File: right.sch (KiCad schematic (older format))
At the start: 59 parts, among them J10 UTC16-G, J4 reset, J5 Speaker, J6 ISP, J8 Sig, P6 WS2812, P8 SJ-43514-SMT, SW25 Socket, SW26 Socket, SW27 Socket, SW28 Socket, SW29 Socket, SW30 Socket, SW31 Socket, SW32 Socket, SW33 Socket, SW34 Socket, SW35 Socket, SW36 Socket, SW37 Socket, SW38 Socket, SW39 Socket, SW40 Socket, SW41 Socket, SW42 Socket, SW43 Socket, SW44 Socket, SW45 Socket, SW46 Socket, SW47 Socket, SW48 Socket, SW50 FSMSM, U2 ATMega32U4, Y2 16MHz

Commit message: Added WS2812B leds to one half
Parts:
- added C? (x6): 1uF, Capacitor_SMD:C_0603_1608Metric, symbol vitamins_included-rescue:C_Small-RESCUE-lets_split_panel-lets_split_panel-rescue
- added D? (x6): WS2812B, LED_SMD:LED_WS2812B_PLCC4_5.0x5.0mm_P3.2mm, symbol LED:WS2812B
- J10: symbol Connector:USB_C_Receptacle -> vitamins_included-rescue:USB_C_Receptacle-Connector
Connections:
- wire segments 187 -> 244

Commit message: started work on second half
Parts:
- gave numbers to parts that had none: 12
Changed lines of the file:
@@
 U 1 1 5C305AB7
 P 7800 4400
-F 0 "D?" H 7875 4650 50  0000 L CNN
+AR Path="/5A0DE9BD/5C305AB7" Ref="D?"  Part="1"
+AR Path="/5A0DF911/5C305AB7" Ref="D35"  Part="1"
+F 0 "D35" H 7875 4650 50  0000 L CNN
 F 1 "WS2812B" H 7875 4150 50  0000 L CNN
 F 2 "LED_SMD:LED_WS2812B_PLCC4_5.0x5.0mm_P3.2mm" H 7850 4100 50  0001 L TNN
@@
 U 1 1 5C305ABE
 P 7350 4200
-F 0 "C?" H 7442 4246 50  0000 L CNN
+AR Path="/5A0DE9BD/5C305ABE" Ref="C?"  Part="1"
+AR Path="/5A0DF911/5C305ABE" Ref="C15"  Part="1"
+F 0 "C15" H 7442 4246 50  0000 L CNN
 F 1 "1uF" H 7442 4155 50  0000 L CNN
 F 2 "Capacitor_SMD:C_0603_1608Metric" H 7350 4200 50  0001 C CNN
@@
 U 1 1 5C305ACC
 P 8750 4400
-F 0 "D?" H 8825 4650 50  0000 L CNN
+AR Path="/5A0DE9BD/5C305ACC" Ref="D?"  Part="1"
+AR Path="/5A0DF911/5C305ACC" Ref="D36"  Part="1"
+F 0 "D36" H 8825 4650 50  0000 L CNN
 F 1 "WS2812B" H 8825 4150 50  0000 L CNN
 F 2 "LED_SMD:LED_WS2812B_PLCC4_5.0x5.0mm_P3.2mm" H 8800 4100 50  0001 L TNN
@@
 U 1 1 5C305AD3
 P 8300 4200
-F 0 "C?" H 8392 4246 50  0000 L CNN
+AR Path="/5A0DE9BD/5C305AD3" Ref="C?"  Part="1"
+AR Path="/5A0DF911/5C305AD3" Ref="C16"  Part="1"
+F 0 "C16" H 8392 4246 50  0000 L CNN
 F 1 "1uF" H 8392 4155 50  0000 L CNN
 F 2 "Capacitor_SMD:C_0603_1608Metric" H 8300 4200 50  0001 C CNN
@@
 U 1 1 5C305AE1
 P 9700 4400
-F 0 "D?" H 9775 4650 50  0000 L CNN
+AR Path="/5A0DE9BD/5C305AE1" Ref="D?"  Part="1"
+AR Path="/5A0DF911/5C305AE1" Ref="D37"  Part="1"
+F 0 "D37" H 9775 4650 50  0000 L CNN
 F 1 "WS2812B" H 9775 4150 50  0000 L CNN
 F 2 "LED_SMD:LED_WS2812B_PLCC4_5.0x5.0mm_P3.2mm" H 9750 4100 50  0001 L TNN
@@
 U 1 1 5C305AE8
 P 9250 4200
-F 0 "C?" H 9342 4246 50  0000 L CNN
+AR Path="/5A0DE9BD/5C305AE8" Ref="C?"  Part="1"
+AR Path="/5A0DF911/5C305AE8" Ref="C17"  Part="1"
+F 0 "C17" H 9342 4246 50  0000 L CNN
 F 1 "1uF" H 9342 4155 50  0000 L CNN
 F 2 "Capacitor_SMD:C_0603_1608Metric" H 9250 4200 50  0001 C CNN
@@
 U 1 1 5C305AF6
 P 7800 5600
-F 0 "D?" H 7875 5850 50  0000 L CNN
+AR Path="/5A0DE9BD/5C305AF6" Ref="D?"  Part="1"
+AR Path="/5A0DF911/5C305AF6" Ref="D38"  Part="1"
+F 0 "D38" H 7875 5850 50  0000 L CNN
 F 1 "WS2812B" H 7875 5350 50  0000 L CNN
 F 2 "LED_SMD:LED_WS2812B_PLCC4_5.0x5.0mm_P3.2mm" H 7850 5300 50  0001 L TNN
@@
 U 1 1 5C305AFD
 P 7350 5400
-F 0 "C?" H 7442 5446 50  0000 L CNN
+AR Path="/5A0DE9BD/5C305AFD" Ref="C?"  Part="1"
+AR Path="/5A0DF911/5C305AFD" Ref="C18"  Part="1"
+F 0 "C18" H 7442 5446 50  0000 L CNN
 F 1 "1uF" H 7442 5355 50  0000 L CNN
 F 2 "Capacitor_SMD:C_0603_1608Metric" H 7350 5400 50  0001 C CNN
@@
 U 1 1 5C305B09
 P 8750 5600
-F 0 "D?" H 8825 5850 50  0000 L CNN
+AR Path="/5A0DE9BD/5C305B09" Ref="D?"  Part="1"
+AR Path="/5A0DF911/5C305B09" Ref="D39"  Part="1"
+F 0 "D39" H 8825 5850 50  0000 L CNN
 F 1 "WS2812B" H 8825 5350 50  0000 L CNN
 F 2 "LED_SMD:LED_WS2812B_PLCC4_5.0x5.0mm_P3.2mm" H 8800 5300 50  0001 L TNN
@@
 U 1 1 5C305B10
 P 8300 5400
-F 0 "C?" H 8392 5446 50  0000 L CNN
+AR Path="/5A0DE9BD/5C305B10" Ref="C?"  Part="1"
+AR Path="/5A0DF911/5C305B10" Ref="C19"  Part="1"
+F 0 "C19" H 8392 5446 50  0000 L CNN
 F 1 "1uF" H 8392 5355 50  0000 L CNN
 F 2 "Capacitor_SMD:C_0603_1608Metric" H 8300 5400 50  0001 C CNN
@@
 U 1 1 5C305B1E
 P 9700 5600
-F 0 "D?" H 9775 5850 50  0000 L CNN
+AR Path="/5A0DE9BD/5C305B1E" Ref="D?"  Part="1"
+AR Path="/5A0DF911/5C305B1E" Ref="D40"  Part="1"
+F 0 "D40" H 9775 5850 50  0000 L CNN
 F 1 "WS2812B" H 9775 5350 50  0000 L CNN
 F 2 "LED_SMD:LED_WS2812B_PLCC4_5.0x5.0mm_P3.2mm" H 9750 5300 50  0001 L TNN
@@
 U 1 1 5C305B25
 P 9250 5400
-F 0 "C?" H 9342 5446 50  0000 L CNN
+AR Path="/5A0DE9BD/5C305B25" Ref="C?"  Part="1"
+AR Path="/5A0DF911/5C305B25" Ref="C20"  Part="1"
+F 0 "C20" H 9342 5446 50  0000 L CNN
 F 1 "1uF" H 9342 5355 50  0000 L CNN
 F 2 "Capacitor_SMD:C_0603_1608Metric" H 9250 5400 50  0001 C CNN
@@
 U 1 1 5C305B43
 P 7350 4000
-F 0 "#PWR?" H 7350 3850 50  0001 C CNN
+AR Path="/5A0DE9BD/5C305B43" Ref="#PWR?"  Part="1"
+AR Path="/5A0DF911/5C305B43" Ref="#PWR0107"  Part="1"
+F 0 "#PWR0107" H 7350 3850 50  0001 C CNN
 F 1 "VCC" H 7350 4150 50  0000 C CNN
 F 2 "" H 7350 4000 50  0000 C CNN
@@
 U 1 1 5C305B4B
 P 7350 5225
-F 0 "#PWR?" H 7350 5075 50  0001 C CNN
+AR Path="/5A0DE9BD/5C305B4B" Ref="#PWR?"  Part="1"
+AR Path="/5A0DF911/5C305B4B" Ref="#PWR0108"  Part="1"
+F 0 "#PWR0108" H 7350 5075 50  0001 C CNN
 F 1 "VCC" H 7350 5375 50  0000 C CNN
 F 2 "" H 7350 5225 50  0000 C CNN
@@
 U 1 1 5C305B54
 P 7350 6000
-F 0 "#PWR?" H 7350 5750 50  0001 C CNN
+AR Path="/5A0DE9BD/5C305B54" Ref="#PWR?"  Part="1"
+AR Path="/5A0DF911/5C305B54" Ref="#PWR0109"  Part="1"
+F 0 "#PWR0109" H 7350 5750 50  0001 C CNN
 F 1 "GND" H 7350 5850 50  0000 C CNN
 F 2 "" H 7350 6000 50  0000 C CNN
@@
 U 1 1 5C305B5C
 P 7350 4800
-F 0 "#PWR?" H 7350 4550 50  0001 C CNN
+AR Path="/5A0DE9BD/5C305B5C" Ref="#PWR?"  Part="1"
+AR Path="/5A0DF911/5C305B5C" Ref="#PWR0110"  Part="1"
+F 0 "#PWR0110" H 7350 4550 50  0001 C CNN
 F 1 "GND" H 7350 4650 50  0000 C CNN
 F 2 "" H 7350 4800 50  0000 C CNN

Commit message: Fixed rotated LEDs, added config jumpers
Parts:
- removed J10: UTC16-G, Connector_USB:USB_C_Receptacle_Palconn_UTC16-G, symbol vitamins_included-rescue:USB_C_Receptacle-Connector
- removed J5: Speaker, Buzzers_Beepers:Buzzer_12x9.5RM7.6, symbol vitamins_included-rescue:Conn_01x02-RESCUE-lets_split_panel-lets_split_panel-re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
- removed J8: Sig, Pin_Headers:Pin_Header_Straight_1x01_Pitch2.54mm, symbol vitamins_included-rescue:Conn_01x01-RESCUE-lets_split_panel-lets_split_panel-re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
- removed P8: SJ-43514-SMT, Connectors:SJ-4351X-SMT, symbol vitamins_included-rescue:Conn_01x04-RESCUE-lets_split_panel-lets_split_panel-re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
- added J10: UTC16-G, Connector_USB:USB_C_Receptacle_Palconn_UTC16-G, symbol Connector:USB_C_Receptacle_USB2.0
- added J5: Buzzer, Buzzers_Beepers:Buzzer_12x9.5RM7.6, symbol Device:Buzzer
- added JP3: WS_MODE, Jumper:SolderJumper-3_P1.3mm_Bridged12_RoundedPad1.0x1.5mm, symbol Jumper:SolderJumper_3_Bridged12
- added JP6: WS_OUT, Jumper:SolderJumper-3_P1.3mm_Bridged12_RoundedPad1.0x1.5mm, symbol Jumper:SolderJumper_3_Bridged12
- added P8: SJ-43514-SMT, UJ31-CH-31-SMT-TR:SJ-4351X-SMT, symbol Connector:AudioJack4
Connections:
- net labels added: WD2812-out
- wire segments 244 -> 239
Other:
- moved on the sheet: C15, C16, C17, C18, C19, C20, D35, D36, D37, D38, D39, D40

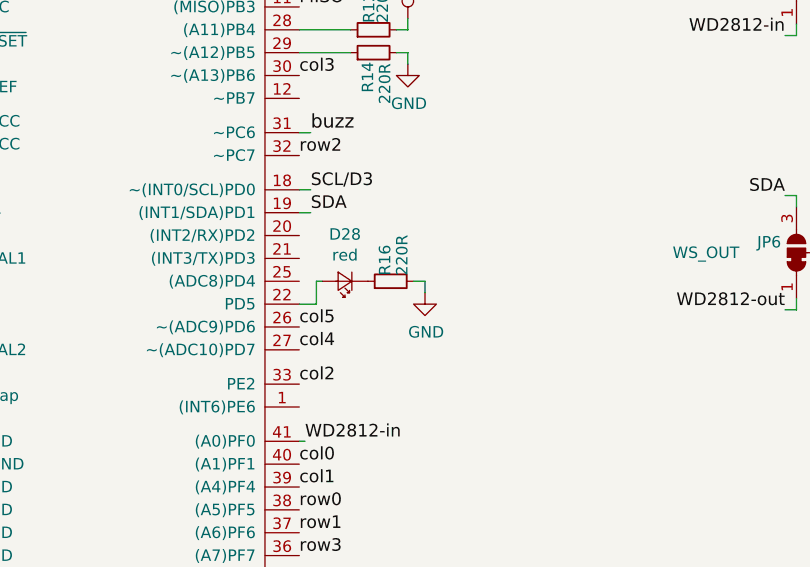
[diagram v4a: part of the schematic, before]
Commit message: Added MPN to DFU LED
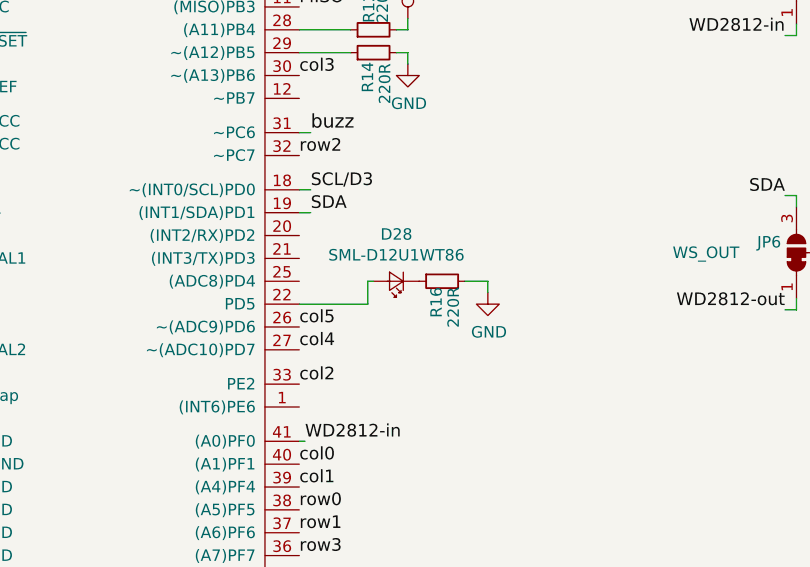
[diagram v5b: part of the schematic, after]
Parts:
- D28: value red -> SML-D12U1WT86
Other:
- moved on the sheet: D28, R16
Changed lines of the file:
@@
 L Device:LED_Small D28
 U 1 1 5B5FD568
-P 5300 5550
-F 0 "D28" H 5300 5345 50  0000 C CNN
-F 1 "red" H 5300 5436 50  0000 C CNN
-F 2 "LED_SMD:LED_0603_1608Metric_Castellated" V 5300 5550 50  0001 C CNN
-F 3 "~" V 5300 5550 50  0001 C CNN
-	1    5300 5550
+P 5525 5550
+F 0 "D28" H 5525 5345 50  0000 C CNN
+F 1 "SML-D12U1WT86" H 5525 5436 50  0000 C CNN
+F 2 "LED_SMD:LED_0603_1608Metric_Castellated" V 5525 5550 50  0001 C CNN
+F 3 "~" V 5525 5550 50  0001 C CNN
+	1    5525 5550
 	-1   0    0    1
 $EndComp
 Wire Wire Line
-	5175 5650 5175 5550
+	5400 5650 5400 5550
 Wire Wire Line
-	5175 5550 5200 5550
+	5400 5550 5425 5550
 $Comp
 L vitamins_included-rescue:R_Small-RESCUE-lets_split_panel-lets_split_panel-rescue R16
 U 1 1 5B5FD571
-P 5500 5550
-F 0 "R16" H 5525 5575 50  0000 L CNN
-F 1 "220R" H 5525 5500 50  0000 L CNN
-F 2 "Resistor_SMD:R_0603_1608Metric" H 5500 5550 50  0001 C CNN
-F 3 "" H 5500 5550 50  0000 C CNN
-	1    5500 5550
-	0    -1   -1   0
+P 5725 5550
+F 0 "R16" H 5750 5575 50  0000 L CNN
+F 1 "220R" H 5750 5500 50  0000 L CNN
+F 2 "Resistor_SMD:R_0603_1608Metric" H 5725 5550 50  0001 C CNN
+F 3 "" H 5725 5550 50  0000 C CNN
+	1    5725 5550
+	0    -1   1    0
 $EndComp
 Wire Wire Line
-	5175 5650 5100 5650
+	5400 5650 5100 5650
 $Comp
 L power:GND #PWR0102
 U 1 1 5B5E458B
-P 5650 5600
-F 0 "#PWR0102" H 5650 5350 50  0001 C CNN
-F 1 "GND" H 5655 5427 50  0000 C CNN
-F 2 "" H 5650 5600 50  0001 C CNN
-F 3 "" H 5650 5600 50  0001 C CNN
-	1    5650 5600
+P 5925 5600
+F 0 "#PWR0102" H 5925 5350 50  0001 C CNN
+F 1 "GND" H 5930 5427 50  0000 C CNN
+F 2 "" H 5925 5600 50  0001 C CNN
+F 3 "" H 5925 5600 50  0001 C CNN
+	1    5925 5600
 	1    0    0    -1
 $EndComp
 Wire Wire Line
-	5600 5550 5650 5550
+	5825 5550 5925 5550
 Wire Wire Line
-	5650 5550 5650 5600
+	5925 5550 5925 5600
 $Comp
 L Connector:AudioJack4 P8

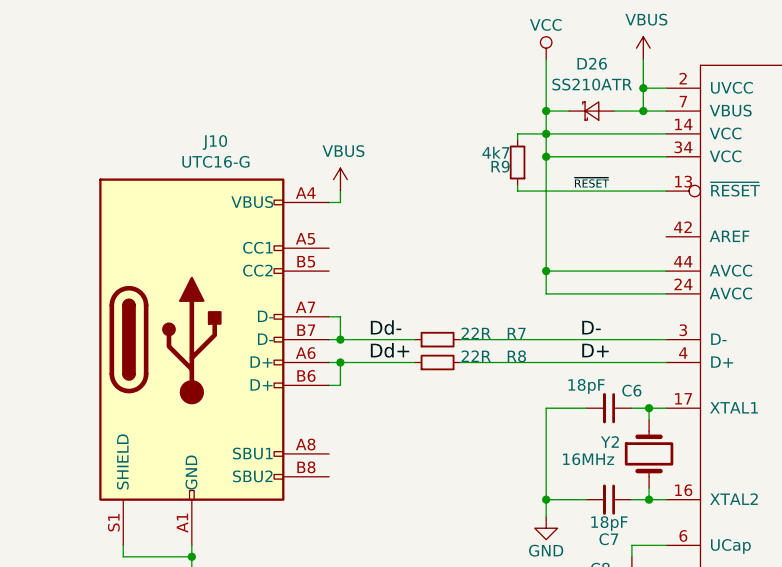
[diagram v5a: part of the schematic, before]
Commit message: Added 5k1 CC resistors
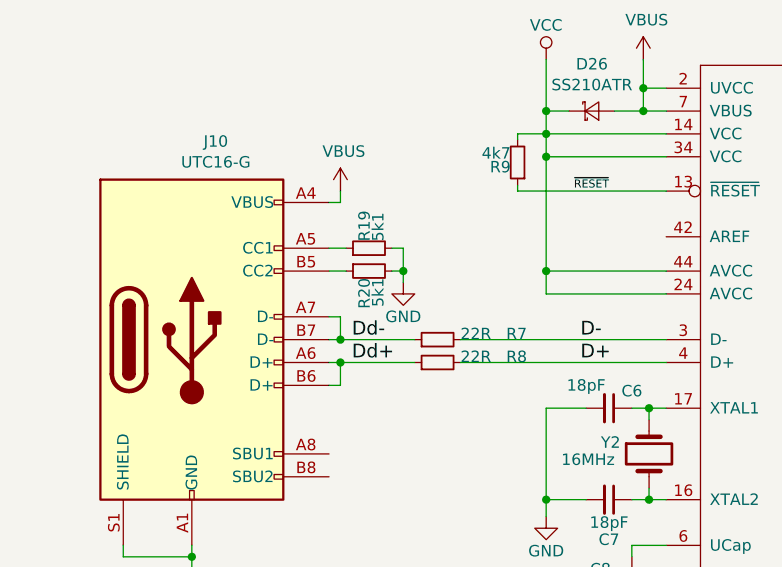
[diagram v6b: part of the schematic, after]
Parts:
- added R19, R20: 5k1, Resistor_SMD:R_0603_1608Metric, symbol vitamins_included-rescue:R_Small-RESCUE-lets_split_panel-lets_split_panel-rescue
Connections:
- net GND: now also R19.2, R20.2
- net at J10.A5 (CC1): now also R19.1
- net at J10.B5 (CC2): now also R20.1
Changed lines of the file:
@@
 Text Label 3250 2050 0    55   ~ 0
 MOSI
-Text Label 2200 5150 0    60   ~ 0
+Text Label 2125 5150 0    60   ~ 0
 Dd-
-Text Label 2200 5250 0    60   ~ 0
+Text Label 2125 5250 0    60   ~ 0
 Dd+
 Text Label 5900 3250 2    60   ~ 0
@@
 Wire Notes Line
 	7575 5500 7500 5425
+$Comp
+L vitamins_included-rescue:R_Small-RESCUE-lets_split_panel-lets_split_panel-rescue R?
+U 1 1 5D2EC9BB
+P 2200 4850
+AR Path="/5A0DE9BD/5D2EC9BB" Ref="R?"  Part="1"
+AR Path="/5A0DF911/5D2EC9BB" Ref="R20"  Part="1"
+F 0 "R20" H 2230 4870 50  0000 L CNN
+F 1 "5k1" H 2230 4810 50  0000 L CNN
+F 2 "Resistor_SMD:R_0603_1608Metric" H 2200 4850 50  0001 C CNN
+F 3 "" H 2200 4850 50  0000 C CNN
+	1    2200 4850
+	0    -1   1    0
+$EndComp
+$Comp
+L vitamins_included-rescue:R_Small-RESCUE-lets_split_panel-lets_split_panel-rescue R?
+U 1 1 5D2EC9C2
+P 2200 4750
+AR Path="/5A0DE9BD/5D2EC9C2" Ref="R?"  Part="1"
+AR Path="/5A0DF911/5D2EC9C2" Ref="R19"  Part="1"
+F 0 "R19" H 2230 4770 50  0000 L CNN
+F 1 "5k1" H 2230 4710 50  0000 L CNN
+F 2 "Resistor_SMD:R_0603_1608Metric" H 2200 4750 50  0001 C CNN
+F 3 "" H 2200 4750 50  0000 C CNN
+	1    2200 4750
+	0    -1   -1   0
+$EndComp
+Wire Wire Line
+	2025 4850 2100 4850
+Wire Wire Line
+	2025 4750 2100 4750
+$Comp
+L vitamins_included-rescue:GND-RESCUE-lets_split_panel-lets_split_panel-rescue #PWR?
+U 1 1 5D2EC9CB
+P 2350 4900
+AR Path="/5A0DE9BD/5D2EC9CB" Ref="#PWR?"  Part="1"
+AR Path="/5A0DF911/5D2EC9CB" Ref="#PWR0112"  Part="1"
+F 0 "#PWR0112" H 2350 4650 50  0001 C CNN
+F 1 "GND" H 2350 4750 50  0000 C CNN
+F 2 "" H 2350 4900 50  0000 C CNN
+F 3 "" H 2350 4900 50  0000 C CNN
+	1    2350 4900
+	1    0    0    -1
+$EndComp
+Wire Wire Line
+	2350 4900 2350 4850
+Wire Wire Line
+	2350 4850 2300 4850
+Wire Wire Line
+	2300 4750 2350 4750
+Wire Wire Line
+	2350 4750 2350 4850
+Connection ~ 2350 4850
 $EndSCHEMATC

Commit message: Pre-cleanup
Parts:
- added J18, J19, J20, J21, J22, J23, J24, J8: Conn_01x01, TestPoint:TestPoint_Pad_D1.5mm, symbol Connector_Generic:Conn_01x01
- R19, R20: value 5k1 -> 5K1
- R9: value 4k7 -> 4K7
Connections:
- net GND: now also J23.1 (Pin_1)
- net VCC: now also J18.1 (Pin_1)
- net PE6: now reaches U2.1 ((INT6)PE6)
- net PE6: now also J20.1 (Pin_1)
- net PB7: now reaches U2.12 (~~PB7)
- net PB7: now also J21.1 (Pin_1)
- net PD2: now reaches U2.20 ((INT2/RX)PD2)
- net PD2: now also J8.1 (Pin_1)
- net PD3: now reaches U2.21 ((INT3/TX)PD3)
- net PD3: now also J19.1 (Pin_1)
- net PD4: now reaches U2.25 ((ADC8)PD4)
- net PD4: now also J24.1 (Pin_1)
- net PB0: now reaches U2.8 ((CS)PB0)
- net PB0: now also J22.1 (Pin_1)
- net WD2812-in renamed WS2812-in
- net WD2812-out renamed WS2812-out
- net ~RESET renamed ~Reset
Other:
- note added: "Connectivity"
- note added: "MCU"
- note added: "Matrix"
- note added: "WS2812B RGB\nUnderglow"
- moved on the sheet: C15, C16, C17, C18, C19, C20, C5, C6, C7, C8, D13, D14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

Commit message: Fixed symbols to not rely on rescue
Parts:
- C15, C16, C17, C18, C19, C20, C5, C6, C7, C8: symbol vitamins_included-rescue:C_Small-RESCUE-lets_split_panel-lets_split_panel-rescue -> Device:C_Small
- J6: symbol vitamins_included-rescue:Conn_02x03_Odd_Even-RESCUE-lets_split_panel-lets_split_panel-rescue -> Connector_Generic:Conn_02x03_Odd_Even
- P6: symbol vitamins_included-rescue:Conn_01x03-RESCUE-lets_split_panel-lets_split_panel-rescue -> Connector_Generic:Conn_01x03
- R10, R12, R14, R16, R19, R20, R7, R8, R9: symbol vitamins_included-rescue:R_Small-RESCUE-lets_split_panel-lets_split_panel-rescue -> Device:R_Small
- SW25, SW26, SW27, SW28, SW29, SW30, SW31, SW32, SW33, SW34, SW35, SW36, SW37, SW38, SW39, SW40, SW41, SW42, SW43, SW44, SW45, SW46, SW47, SW48: symbol vitamins_included-rescue:SW_Push-RESCUE-lets_split_panel-lets_split_panel-rescue -> Switch:SW_Push
- U2: symbol vitamins_included-rescue:ATMega32U4-RESCUE-lets_split_panel-lets_split_panel-rescue -> 8Bit-MCU:ATMega32U4
- Y2: symbol vitamins_included-rescue:Crystal-RESCUE-lets_split_panel-lets_split_panel-rescue -> Device:Crystal
